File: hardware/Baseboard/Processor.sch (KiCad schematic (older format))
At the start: 25 parts, among them IC1 74HC00, IC10 W65C22, IC2 W65C02, IC3 74HC138, IC4 SYSTEM ROM, IC5 RAM, IC6 W65C22, IC7 W65C51, SW6 CLOCK, SW7 CLOCK INPUT

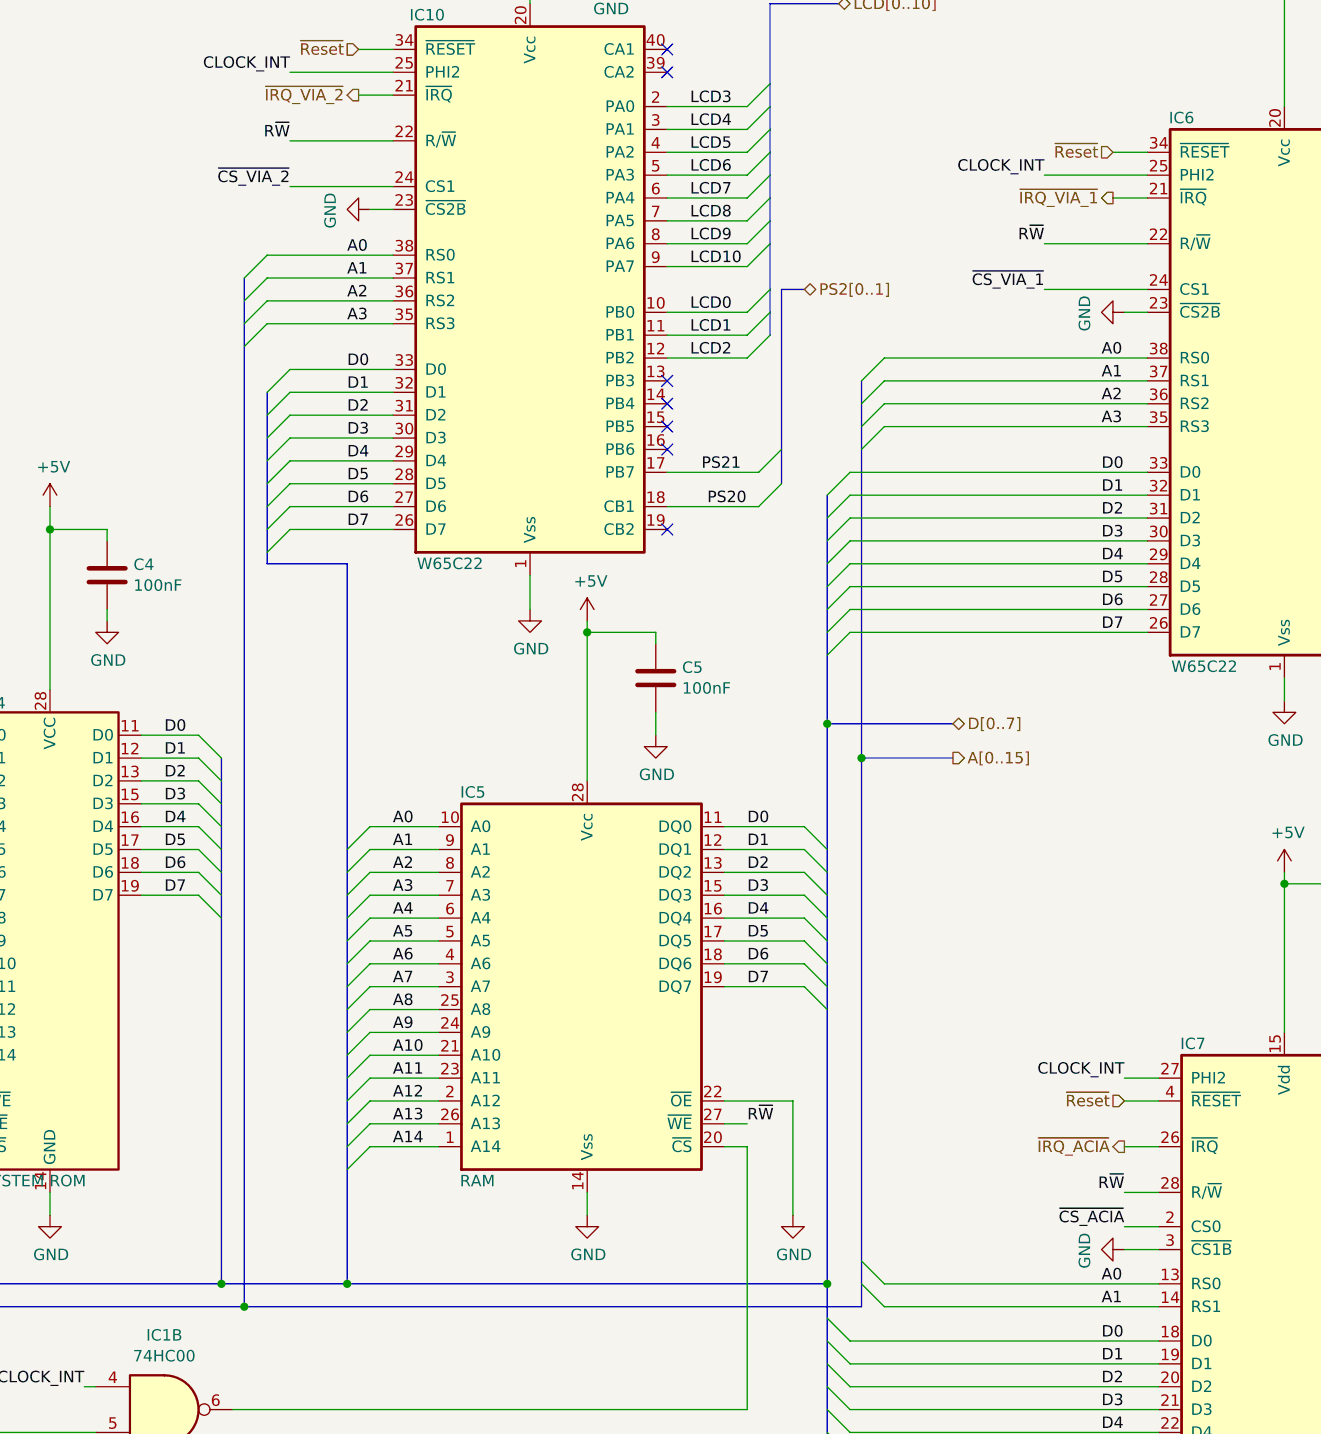
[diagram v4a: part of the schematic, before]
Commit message: Move CS signals for peripheral devices to not(CS) pins
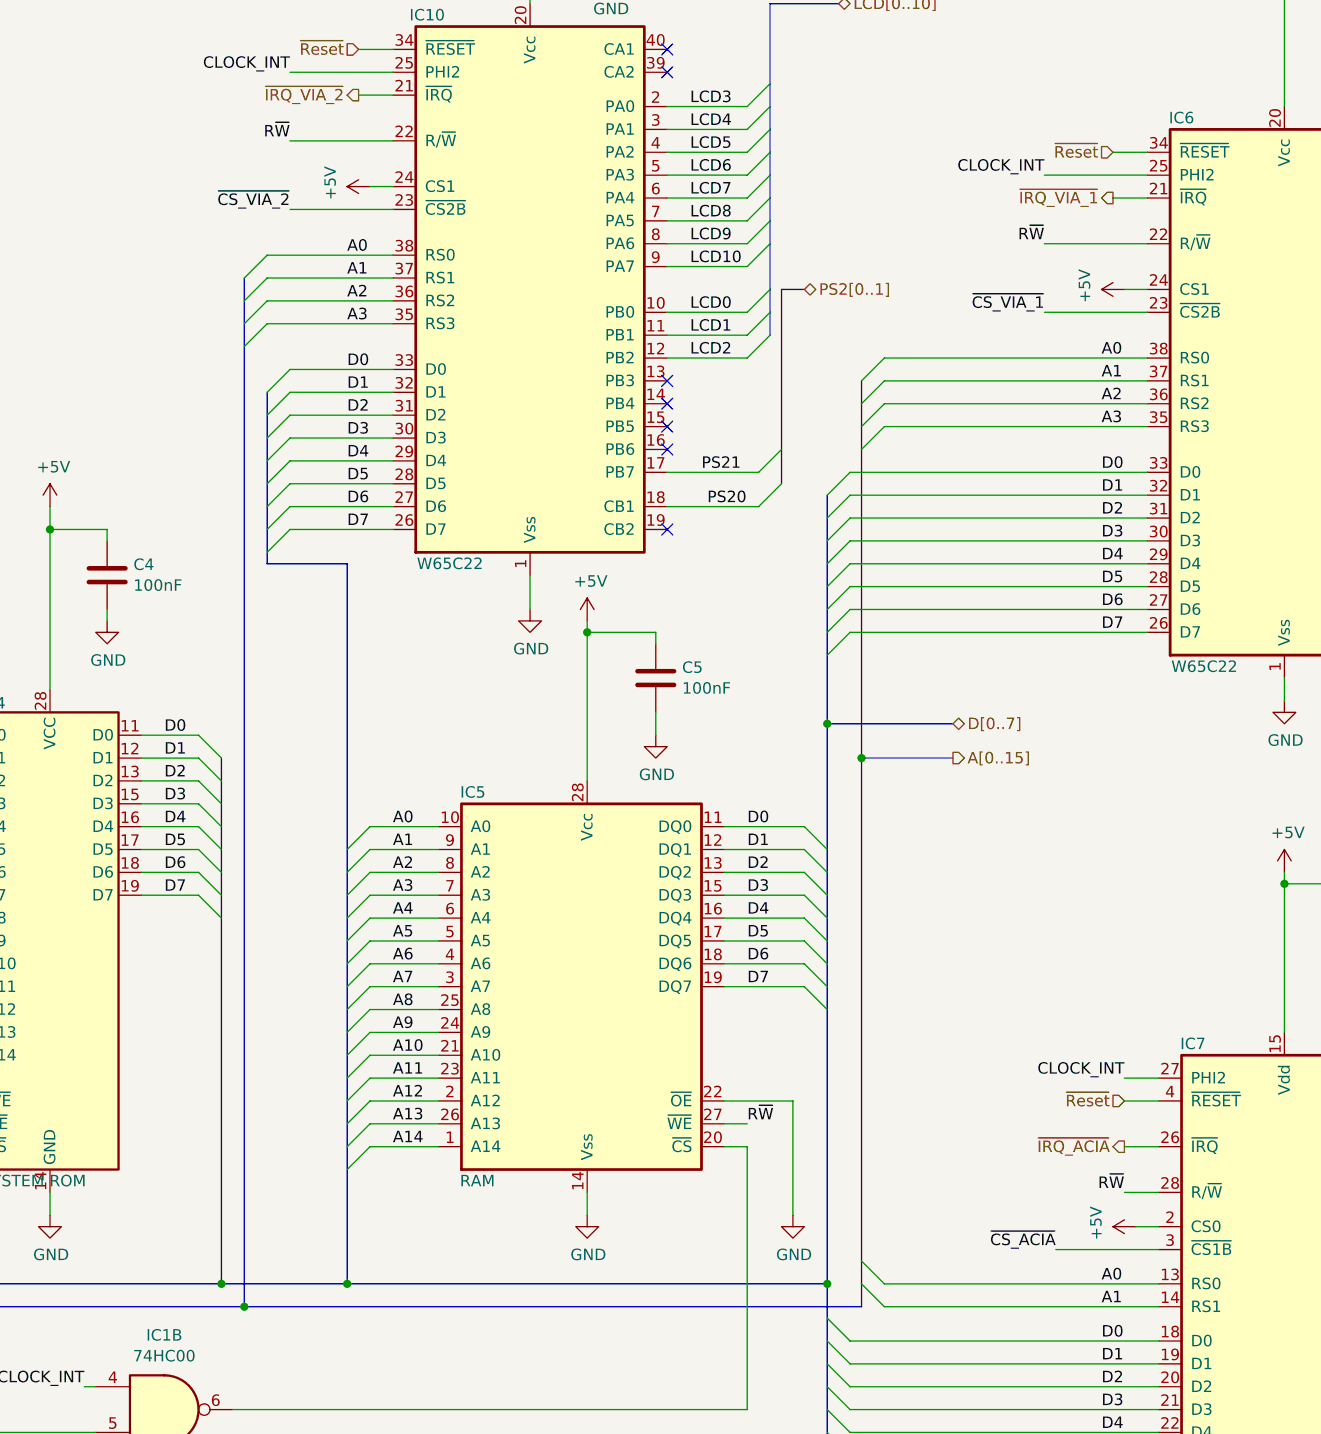
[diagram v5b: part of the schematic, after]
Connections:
- net +5V: now also IC10.24 (CS1), IC6.24 (CS1), IC7.2 (CS0)
- net GND: no longer IC10.23 (~CS2B), IC6.23 (~CS2B), IC7.3 (~CS1B)
- net ~CS_ACIA: now also IC7.3 (~CS1B); no longer IC7.2 (CS0)
- net ~CS_VIA_1: now also IC6.23 (~CS2B); no longer IC6.24 (CS1)
- net ~CS_VIA_2: now also IC10.23 (~CS2B); no longer IC10.24 (CS1)
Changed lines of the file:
@@
 Text Label 5750 9925 0    50   ~ 0
 ~CS_ACIA
-Text Label 12700 6775 2    50   ~ 0
-~CS_ACIA
-Wire Wire Line
-	12850 6775 12700 6775
 $Comp
 L 74xx:74HC00 IC1
@@
 Wire Wire Line
 	11250 6225 11250 6725
-$Comp
-L power:GND #PWR?
-U 1 1 5DF61328
-P 12700 6875
-AR Path="/5DF61328" Ref="#PWR?"  Part="1"
-AR Path="/5EB09E21/5DF61328" Ref="#PWR025"  Part="1"
-F 0 "#PWR025" H 12700 6625 50  0001 C CNN
-F 1 "GND" H 12705 6702 50  0000 C CNN
-F 2 "" H 12700 6875 50  0001 C CNN
-F 3 "" H 12700 6875 50  0001 C CNN
-	1    12700 6875
-	0    1    1    0
-$EndComp
-Wire Wire Line
-	12700 6875 12850 6875
-$Comp
-L power:GND #PWR?
-U 1 1 5DF78C36
-P 12700 2775
-AR Path="/5DF78C36" Ref="#PWR?"  Part="1"
-AR Path="/5EB09E21/5DF78C36" Ref="#PWR024"  Part="1"
-F 0 "#PWR024" H 12700 2525 50  0001 C CNN
-F 1 "GND" H 12705 2602 50  0000 C CNN
-F 2 "" H 12700 2775 50  0001 C CNN
-F 3 "" H 12700 2775 50  0001 C CNN
-	1    12700 2775
-	0    1    1    0
-$EndComp
-Wire Wire Line
-	12700 2775 12800 2775
-Wire Wire Line
-	12800 2675 12350 2675
-Text Label 12350 2675 2    50   ~ 0
-~CS_VIA_1
 Text HLabel 5800 4825 2    50   Input ~ 0
 ~NMI
@@
 Wire Wire Line
 	9350 1625 9500 1625
-$Comp
-L power:GND #PWR?
-U 1 1 5DD17184
-P 9400 2325
-AR Path="/5DD17184" Ref="#PWR?"  Part="1"
-AR Path="/5EB09E21/5DD17184" Ref="#PWR013"  Part="1"
-F 0 "#PWR013" H 9400 2075 50  0001 C CNN
-F 1 "GND" H 9405 2152 50  0000 C CNN
-F 2 "" H 9400 2325 50  0001 C CNN
-F 3 "" H 9400 2325 50  0001 C CNN
-	1    9400 2325
-	0    1    1    0
-$EndComp
-Wire Wire Line
-	9400 2325 9500 2325
-Wire Wire Line
-	9500 2225 9050 2225
-Text Label 9050 2225 2    50   ~ 0
-~CS_VIA_2
 Text Label 5750 9825 0    50   ~ 0
 ~CS_VIA_2
@@
 Wire Wire Line
 	5750 4725 6350 4725
+Wire Wire Line
+	12800 2775 12350 2775
+Text Label 12350 2775 2    50   ~ 0
+~CS_VIA_1
+Wire Wire Line
+	12700 2675 12800 2675
+$Comp
+L power:+5V #PWR?
+U 1 1 5E1808C3
+P 12700 2675
+AR Path="/5E1808C3" Ref="#PWR?"  Part="1"
+AR Path="/5EB09E21/5E1808C3" Ref="#PWR?"  Part="1"
+F 0 "#PWR?" H 12700 2525 50  0001 C CNN
+F 1 "+5V" H 12715 2848 50  0000 C CNN
+F 2 "" H 12700 2675 50  0001 C CNN
+F 3 "" H 12700 2675 50  0001 C CNN
+	1    12700 2675
+	0    -1   -1   0
+$EndComp
+Wire Wire Line
+	9500 2325 9050 2325
+Text Label 9050 2325 2    50   ~ 0
+~CS_VIA_2
+Wire Wire Line
+	9400 2225 9500 2225
+$Comp
+L power:+5V #PWR?
+U 1 1 5E1E7B71
+P 9400 2225
+AR Path="/5E1E7B71" Ref="#PWR?"  Part="1"
+AR Path="/5EB09E21/5E1E7B71" Ref="#PWR?"  Part="1"
+F 0 "#PWR?" H 9400 2075 50  0001 C CNN
+F 1 "+5V" H 9415 2398 50  0000 C CNN
+F 2 "" H 9400 2225 50  0001 C CNN
+F 3 "" H 9400 2225 50  0001 C CNN
+	1    9400 2225
+	0    -1   -1   0
+$EndComp
+Wire Wire Line
+	12850 6875 12400 6875
+Text Label 12400 6875 2    50   ~ 0
+~CS_ACIA
+Wire Wire Line
+	12750 6775 12850 6775
+$Comp
+L power:+5V #PWR?
+U 1 1 5E20A942
+P 12750 6775
+AR Path="/5E20A942" Ref="#PWR?"  Part="1"
+AR Path="/5EB09E21/5E20A942" Ref="#PWR?"  Part="1"
+F 0 "#PWR?" H 12750 6625 50  0001 C CNN
+F 1 "+5V" H 12765 6948 50  0000 C CNN
+F 2 "" H 12750 6775 50  0001 C CNN
+F 3 "" H 12750 6775 50  0001 C CNN
+	1    12750 6775
+	0    -1   -1   0
+$EndComp
 Wire Bus Line
 	11200 2675 11200 3525

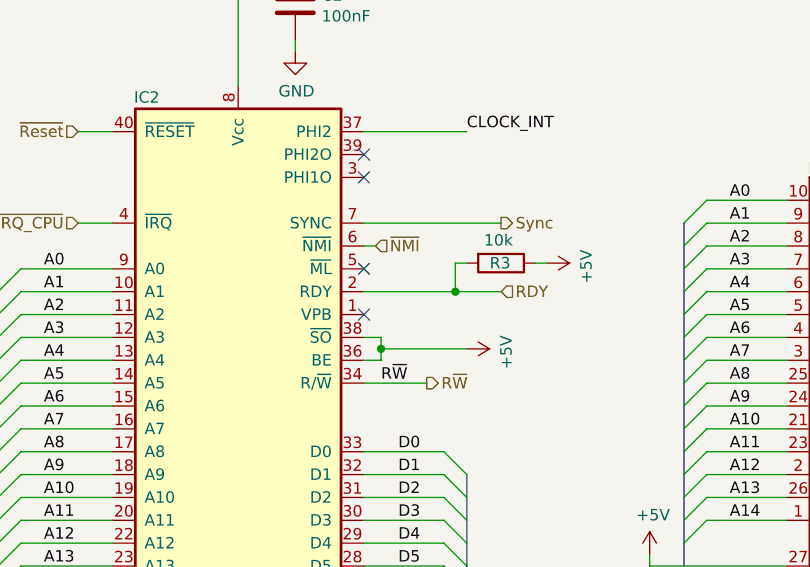
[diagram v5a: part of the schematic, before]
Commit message: Add VP signal to expansion header, optimize routing
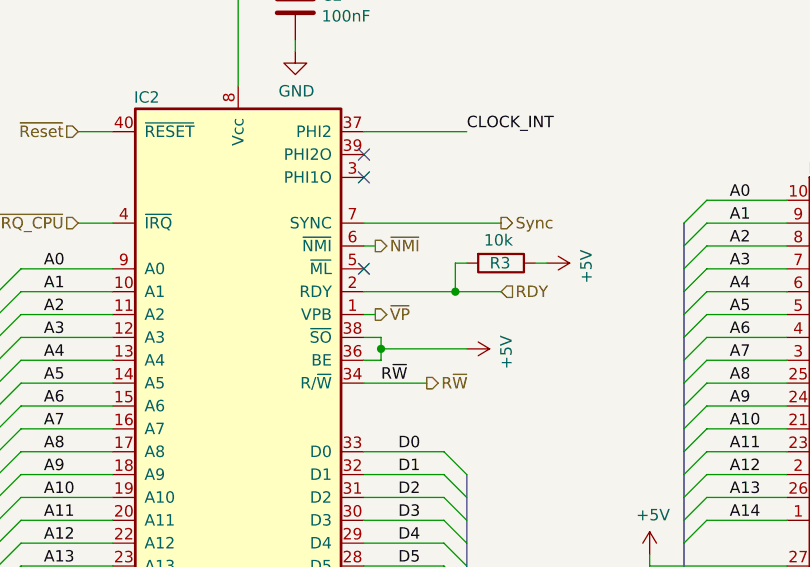
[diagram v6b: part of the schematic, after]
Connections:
- net ~VP: now reaches IC2.1 (VPB)
- no-connect marks 20 -> 19
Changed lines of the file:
@@
 Wire Wire Line
 	11250 6225 11250 6725
-Text HLabel 5800 4825 2    50   Input ~ 0
+Text HLabel 5800 4825 2    50   Output ~ 0
 ~NMI
 Wire Wire Line
@@
 Wire Wire Line
 	6150 5025 5750 5025
-NoConn ~ 5750 5125
 Wire Wire Line
 	6200 4900 6150 4900
@@
 P 12700 2675
 AR Path="/5E1808C3" Ref="#PWR?"  Part="1"
-AR Path="/5EB09E21/5E1808C3" Ref="#PWR?"  Part="1"
-F 0 "#PWR?" H 12700 2525 50  0001 C CNN
+AR Path="/5EB09E21/5E1808C3" Ref="#PWR0109"  Part="1"
+F 0 "#PWR0109" H 12700 2525 50  0001 C CNN
 F 1 "+5V" H 12715 2848 50  0000 C CNN
 F 2 "" H 12700 2675 50  0001 C CNN
@@
 P 9400 2225
 AR Path="/5E1E7B71" Ref="#PWR?"  Part="1"
-AR Path="/5EB09E21/5E1E7B71" Ref="#PWR?"  Part="1"
-F 0 "#PWR?" H 9400 2075 50  0001 C CNN
+AR Path="/5EB09E21/5E1E7B71" Ref="#PWR0110"  Part="1"
+F 0 "#PWR0110" H 9400 2075 50  0001 C CNN
 F 1 "+5V" H 9415 2398 50  0000 C CNN
 F 2 "" H 9400 2225 50  0001 C CNN
@@
 P 12750 6775
 AR Path="/5E20A942" Ref="#PWR?"  Part="1"
-AR Path="/5EB09E21/5E20A942" Ref="#PWR?"  Part="1"
-F 0 "#PWR?" H 12750 6625 50  0001 C CNN
+AR Path="/5EB09E21/5E20A942" Ref="#PWR0111"  Part="1"
+F 0 "#PWR0111" H 12750 6625 50  0001 C CNN
 F 1 "+5V" H 12765 6948 50  0000 C CNN
 F 2 "" H 12750 6775 50  0001 C CNN
@@
 	0    -1   -1   0
 $EndComp
+Text HLabel 5800 5125 2    50   Output ~ 0
+~VP
+Wire Wire Line
+	5800 5125 5750 5125
 Wire Bus Line
 	11200 2675 11200 3525

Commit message: Working on PCB
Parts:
- removed C19, C4: 100nF, Capacitor_THT:C_Rect_L4.0mm_W2.5mm_P2.50mm, symbol Device:C
- removed R10: 10k, Resistor_THT:R_Axial_DIN0207_L6.3mm_D2.5mm_P7.62mm_Horizontal, symbol Device:R
- removed SW6: CLOCK, Button_Switch_THT:SW_PUSH_6mm_H4.3mm, symbol Switch:SW_Push
- added X6: EXT. CLOCK, Connector_Coaxial:MMCX_Molex_73415-1471_Vertical, symbol Connector_Generic:Conn_01x02
- IC4: Mouser 556-AT28C256-15PU -> 556-AT28C25615PU
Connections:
- net GND: now also X6.2 (Pin_2)
- net CLOCK_BTN renamed CLOCK_EXT
- net CLOCK_EXT: now also X6.1 (Pin_1)
- net CLOCK_OSC renamed CLOCK_INT
- net CTS renamed ~CTS
- net RTS renamed ~RTS
- net ~CarrierDetect renamed ~DCD
- net ~ModemReady renamed ~DSR
- net ~TerminalReady renamed ~DTR
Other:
- moved on the sheet: C18, C2, C5, C6, C7, R3

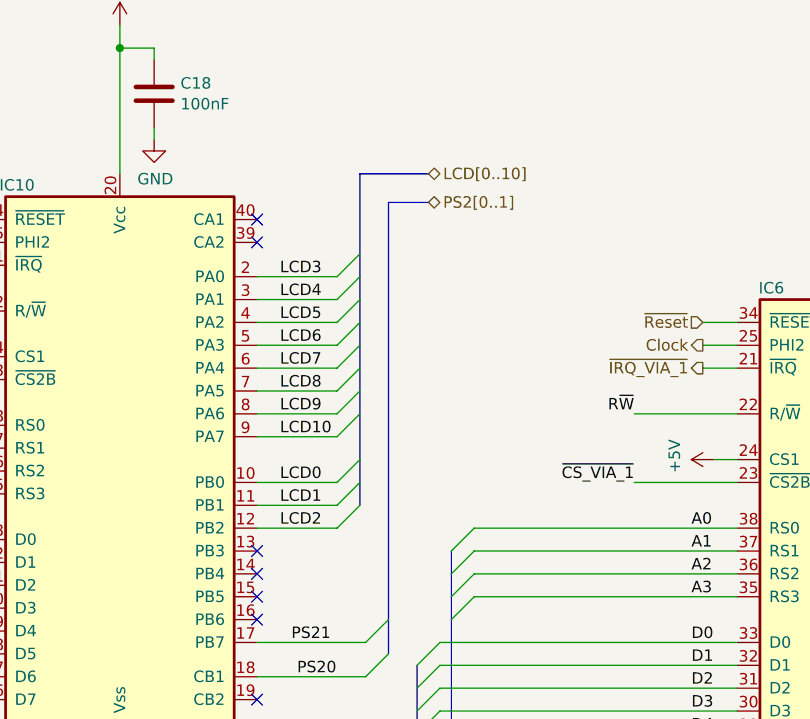
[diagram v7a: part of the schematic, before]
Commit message: Add pull up resistors for PS/2, add LCD backlight switch
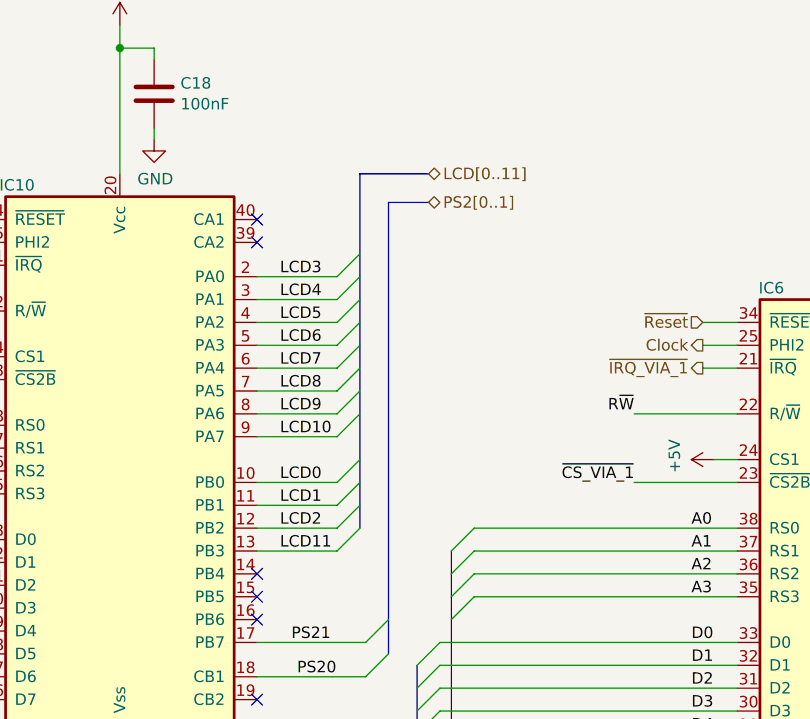
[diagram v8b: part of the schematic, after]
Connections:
- net LCD11: now reaches IC10.13 (PB3)
- no-connect marks 19 -> 18
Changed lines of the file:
@@
 A2
 Text HLabel 11450 1425 2    50   BiDi ~ 0
-LCD[0..10]
+LCD[0..11]
 Wire Bus Line
 	11400 4575 11950 4575
@@
 ~IRQ_CPU
 NoConn ~ 10700 3375
-NoConn ~ 10700 3075
 $Comp
 L Device:R R?
@@
 Text HLabel 9350 1725 0    50   Output ~ 0
 Clock
+Wire Wire Line
+	10700 3075 11050 3075
+Text Label 10800 3075 0    50   ~ 0
+LCD11
+Entry Wire Line
+	11050 3075 11150 2975
 Wire Bus Line
 	11275 1550 11275 3525
@@
 	14350 2225 14350 2925
 Wire Bus Line
-	11150 1425 11150 2875
-Wire Bus Line
 	11400 7025 11400 7875
 Wire Bus Line
@@
 	6200 5825 6200 7025
 Wire Bus Line
+	11150 1425 11150 2975
+Wire Bus Line
 	4150 5025 4150 7125
